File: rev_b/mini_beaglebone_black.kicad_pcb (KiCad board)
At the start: 2 copper layers, 50 x 50 mm, 18 parts, among them Q1 PN2222, U1 74X125, U2 74HCT08

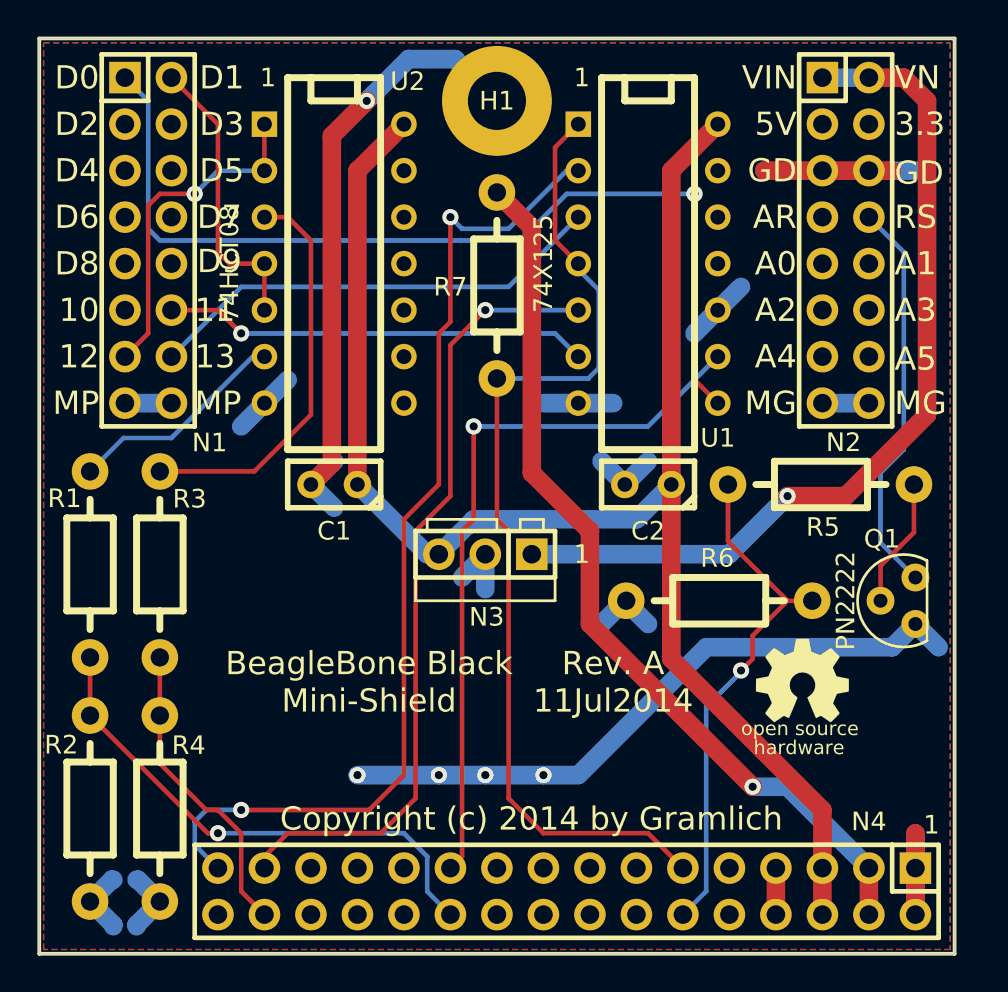
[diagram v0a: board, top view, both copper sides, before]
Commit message: Moved R3 and R4
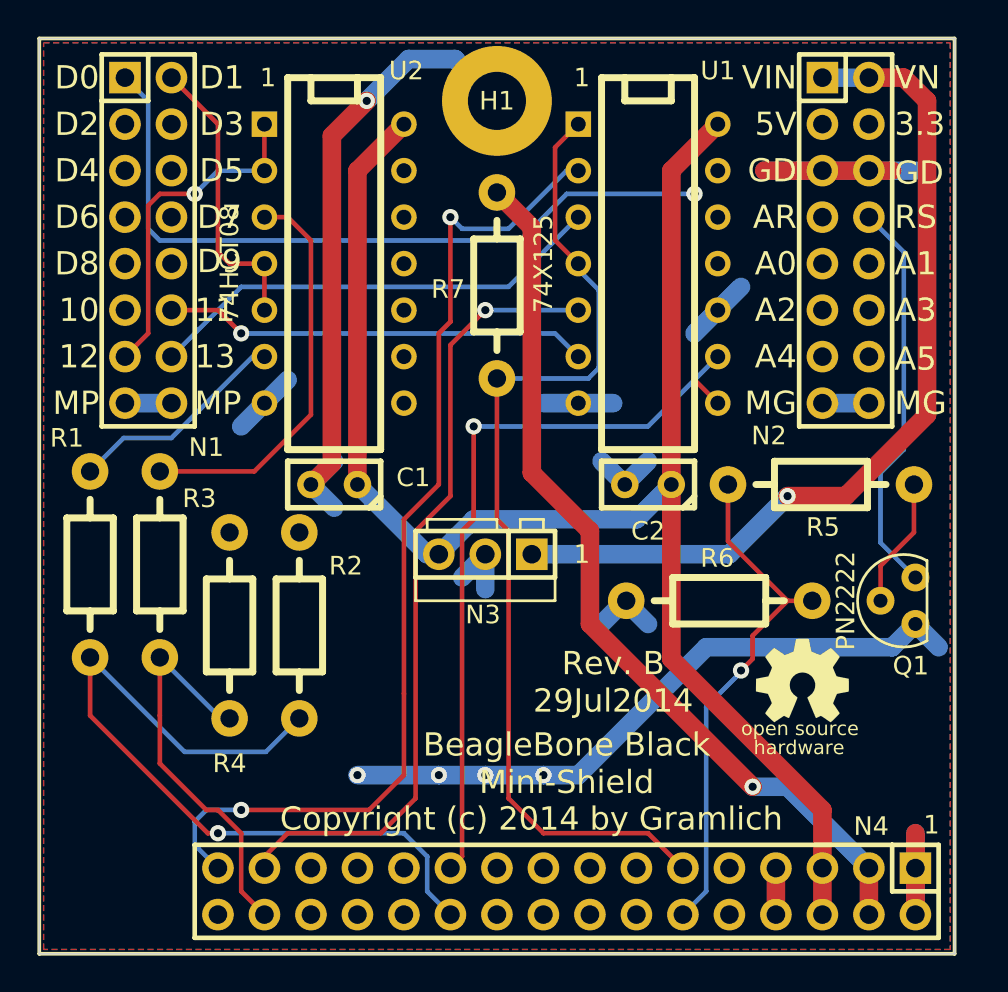
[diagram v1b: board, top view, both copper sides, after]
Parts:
- C1, C2: footprint Mini_BeagleBone_Black_Rev_A:Capacitor3MMDiscRM2.5 -> Mini_BeagleBone_Black_Rev_B:Capacitor3MMDiscRM2.5
- G1: footprint Mini_BeagleBone_Black_Rev_A:OSHW_LOGO_200mil -> Mini_BeagleBone_Black_Rev_B:OSHW_LOGO_200mil
- H1: footprint Mini_BeagleBone_Black_Rev_A:MountingHole_3mm -> Mini_BeagleBone_Black_Rev_B:MountingHole_3mm
- N1, N2: footprint Mini_BeagleBone_Black_Rev_A:Pin_Header_Straight_2x08 -> Mini_BeagleBone_Black_Rev_B:Pin_Header_Straight_2x08
- N3: footprint Mini_BeagleBone_Black_Rev_A:OKI_DC_TO_DC_CONNECTOR -> Mini_BeagleBone_Black_Rev_B:OKI_DC_TO_DC_CONNECTOR
- N4: footprint Mini_BeagleBone_Black_Rev_A:Pin_Header_Straight_2x16 -> Mini_BeagleBone_Black_Rev_B:Pin_Header_Straight_2x16
- Q1: footprint Mini_BeagleBone_Black_Rev_A:TO92_123 -> Mini_BeagleBone_Black_Rev_B:TO92_123
- R1, R2, R3, R4, R5, R6, R7: footprint Mini_BeagleBone_Black_Rev_A:Resistor_Horizontal_RM10mm -> Mini_BeagleBone_Black_Rev_B:Resistor_Horizontal_RM10mm
- U1, U2: footprint Mini_BeagleBone_Black_Rev_A:DIP-14__300 -> Mini_BeagleBone_Black_Rev_B:DIP-14__300
- moved R2 15.3 mm to (90.8, 135.3), turned to 270 degrees
- moved R4 10.9 mm to (87.0, 135.3), turned to 270 degrees
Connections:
- N1 pad 10: (no net) -> /D9
- N1 pad 11: (no net) -> /D10
- N1 pad 3: (no net) -> /D2
- N1 pad 4: (no net) -> /D3
- N1 pad 5: (no net) -> /D4
- N1 pad 6: (no net) -> /D5
- N1 pad 7: (no net) -> /D6
- N1 pad 8: (no net) -> /D7
- N1 pad 9: (no net) -> /D8
- N2 pad 10: (no net) -> /A1
- N2 pad 11: (no net) -> /A2
- N2 pad 12: (no net) -> /A3
- N2 pad 13: (no net) -> /A4
- N2 pad 14: (no net) -> /A5
- N2 pad 3: (no net) -> /5V
- N2 pad 4: (no net) -> /3V3
- N2 pad 7: (no net) -> /AREF
- N2 pad 9: (no net) -> /A0
- N4 pad 10: (no net) -> Net-(N4-Pad10)
- N4 pad 13: (no net) -> Net-(N4-Pad13)
- N4 pad 14: (no net) -> Net-(N4-Pad14)
- N4 pad 15: (no net) -> Net-(N4-Pad15)
- N4 pad 16: (no net) -> Net-(N4-Pad16)
- N4 pad 17: (no net) -> Net-(N4-Pad17)
- N4 pad 18: (no net) -> Net-(N4-Pad18)
- N4 pad 19: (no net) -> Net-(N4-Pad19)
- N4 pad 20: (no net) -> Net-(N4-Pad20)
- N4 pad 23: (no net) -> Net-(N4-Pad23)
- N4 pad 24: (no net) -> Net-(N4-Pad24)
- N4 pad 25: (no net) -> Net-(N4-Pad25)
- N4 pad 26: (no net) -> Net-(N4-Pad26)
- N4 pad 27: (no net) -> Net-(N4-Pad27)
- N4 pad 28: (no net) -> Net-(N4-Pad28)
- N4 pad 32: (no net) -> Net-(N4-Pad32)
- N4 pad 9: (no net) -> Net-(N4-Pad9)
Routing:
- net Net-(N4-Pad22): track 28.5 -> 42.8 mm
- net GND: track 123.7 -> 116.5 mm
- net Net-(N4-Pad30): track 16.8 -> 22.0 mm
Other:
- board text added: "Rev. B 29Jul2014"
- board text removed: "Rev. A 11Jul2014"
- board text removed: "Rev. A1 11Jul2014"
